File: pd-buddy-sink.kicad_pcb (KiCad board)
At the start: 4 copper layers, 30 x 25 mm, 43 parts, among them J1 5-20 V⎓, J2 USB_C_Receptacle, P1 SWD, Q1 MMBT2222ALT1G, Q2 DMP4015SSS, SW1 Boot, SW2 Setup, U1 AP2204R-3.3TRG1, U2 STM32F072C8Ux, U3 FUSB302BMPX

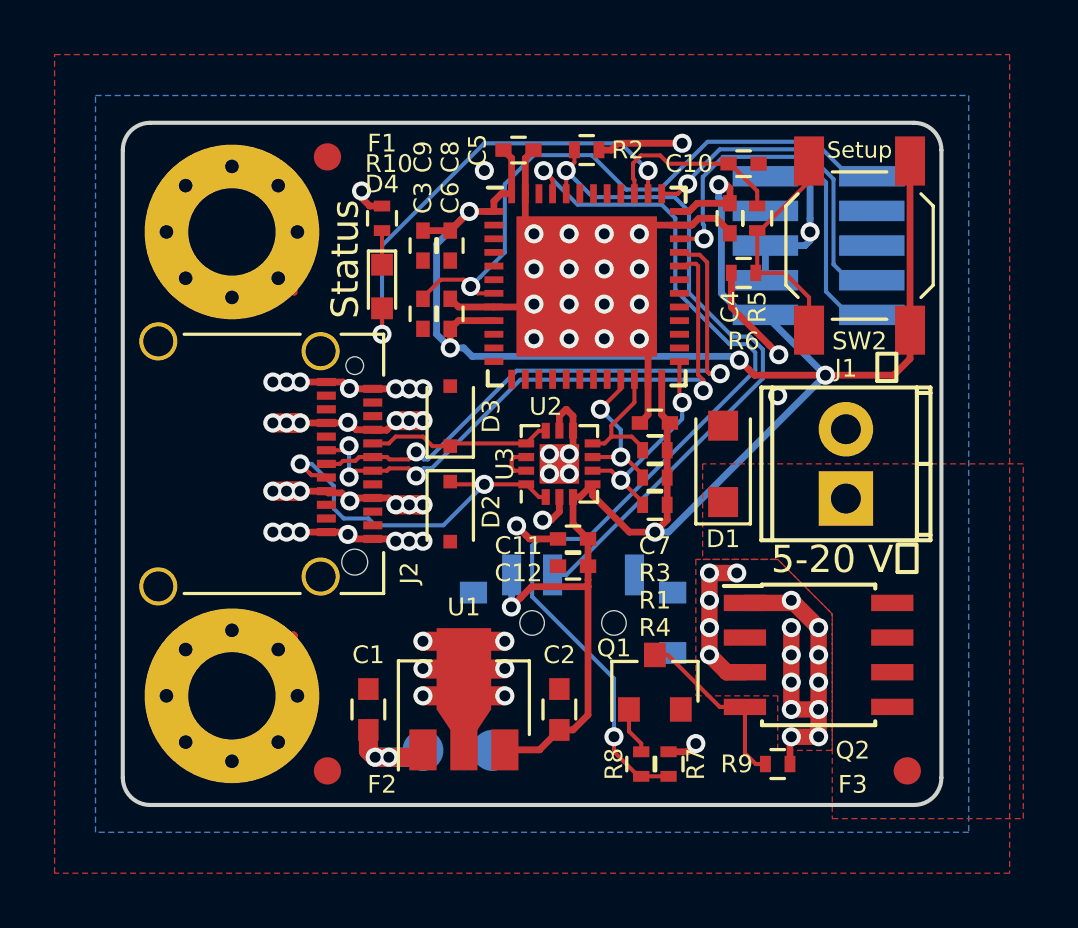
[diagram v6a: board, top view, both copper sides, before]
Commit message: Change part for D2 and D3
Now they're MM3Z5V6T1G, an SOD-323 5.6 V 300 mW Zener diode.  Similar to
the old part, but easier to solder and cheaper.  One of those two points
matters.
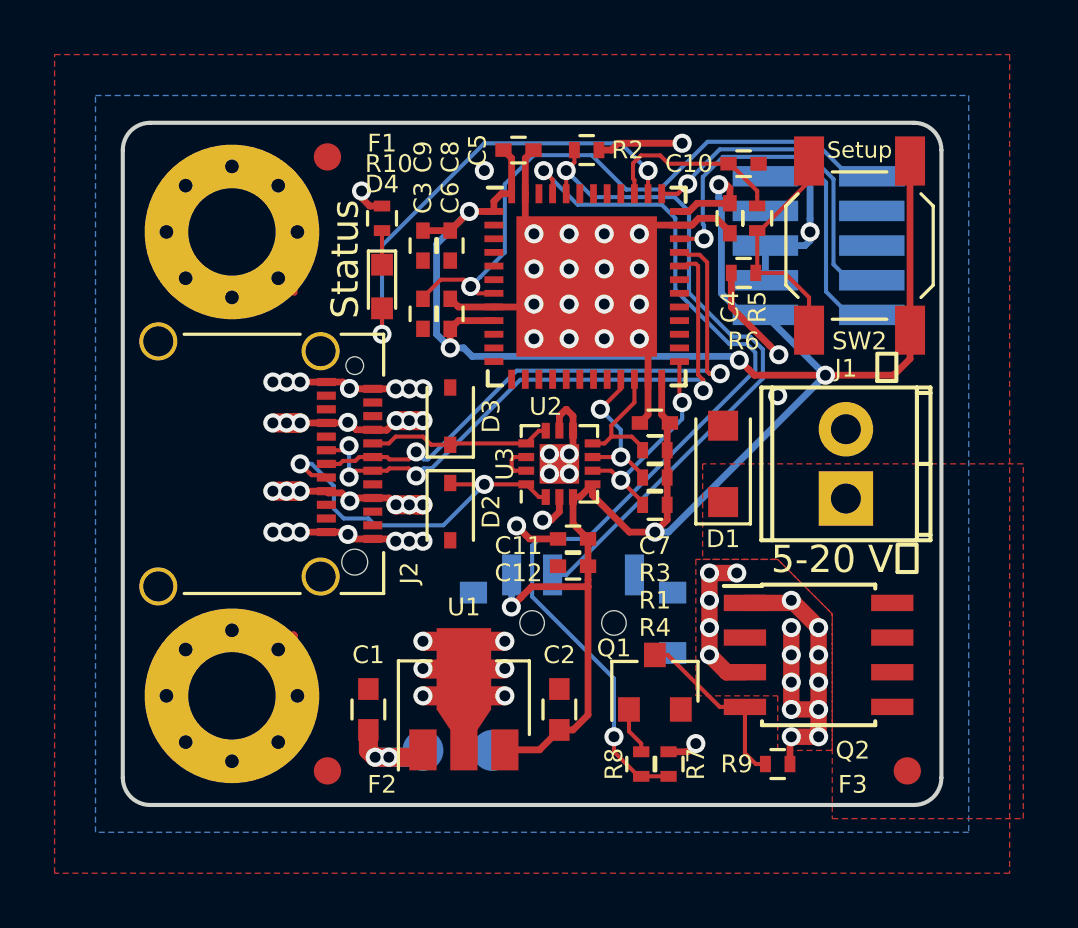
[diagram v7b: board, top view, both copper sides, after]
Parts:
- D2, D3: value CZRF52C5V6 -> MM3Z5V6T1G; footprint Diodes_SMD:D_SOD-323F -> Diodes_SMD:D_SOD-323
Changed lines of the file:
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@@
       (net 2 GND))
   )
-  (module Diodes_SMD:D_SOD-323F (layer F.Cu)
+  (module Diodes_SMD:D_SOD-323 (layer F.Cu)
     (at 93.5 71.75 270)
-    (descr "SOD-323F http://www.nxp.com/documents/outline_drawing/SOD323F.pdf")
-    (tags SOD-323F)
+    (descr SOD-323)
+    (tags SOD-323)
     (attr smd)
-    (fp_text reference D2 (at 0 -1.5 450) (layer F.SilkS)
+    (fp_text reference D2 (at 0 -1.5 270) (layer F.SilkS)
       (effects (font (size 0.65 0.65) (thickness 0.12)))
     )
-    (fp_text value CZRF52C5V6 (at 0.1 1.9 270) (layer F.Fab)
+    (fp_text value MM3Z5V6T1G (at 0.1 1.9 270) (layer F.Fab)
       (effects (font (size 1 1) (thickness 0.15)))
     )
@@
     (fp_line (start -1.5 0.85) (end 1.05 0.85) (layer F.SilkS) (width 0.12))
     (fp_line (start -1.5 -0.85) (end 1.05 -0.85) (layer F.SilkS) (width 0.12))
-    (pad 1 smd rect (at -1.1 0 270) (size 0.5 0.5) (layers F.Cu F.Paste F.Mask)
+    (pad 1 smd rect (at -1.05 0 270) (size 0.6 0.45) (layers F.Cu F.Paste F.Mask)
       (net 5 "/PD PHY/CC2"))
-    (pad 2 smd rect (at 1.1 0 270) (size 0.5 0.5) (layers F.Cu F.Paste F.Mask)
+    (pad 2 smd rect (at 1.05 0 270) (size 0.6 0.45) (layers F.Cu F.Paste F.Mask)
       (net 2 GND))
-    (model ${KISYS3DMOD}/Diodes_SMD.3dshapes/D_SOD-323F.wrl
+    (model ${KISYS3DMOD}/Diodes_SMD.3dshapes/D_SOD-323.wrl
       (at (xyz 0 0 0))
       (scale (xyz 1 1 1))
@@
     )
   )
-  (module Diodes_SMD:D_SOD-323F (layer F.Cu)
+  (module Diodes_SMD:D_SOD-323 (layer F.Cu)
     (at 93.5 68.25 90)
-    (descr "SOD-323F http://www.nxp.com/documents/outline_drawing/SOD323F.pdf")
-    (tags SOD-323F)
+    (descr SOD-323)
+    (tags SOD-323)
     (attr smd)
     (fp_text reference D3 (at 0 1.5 90) (layer F.SilkS)
       (effects (font (size 0.65 0.65) (thickness 0.12)))
     )
-    (fp_text value CZRF52C5V6 (at 0.1 1.9 90) (layer F.Fab)
+    (fp_text value MM3Z5V6T1G (at 0.1 1.9 90) (layer F.Fab)
       (effects (font (size 1 1) (thickness 0.15)))
     )
@@
     (fp_line (start -1.5 0.85) (end 1.05 0.85) (layer F.SilkS) (width 0.12))
     (fp_line (start -1.5 -0.85) (end 1.05 -0.85) (layer F.SilkS) (width 0.12))
-    (pad 1 smd rect (at -1.1 0 90) (size 0.5 0.5) (layers F.Cu F.Paste F.Mask)
+    (pad 1 smd rect (at -1.05 0 90) (size 0.6 0.45) (layers F.Cu F.Paste F.Mask)
       (net 6 "/PD PHY/CC1"))
-    (pad 2 smd rect (at 1.1 0 90) (size 0.5 0.5) (layers F.Cu F.Paste F.Mask)
+    (pad 2 smd rect (at 1.05 0 90) (size 0.6 0.45) (layers F.Cu F.Paste F.Mask)
       (net 2 GND))
-    (model ${KISYS3DMOD}/Diodes_SMD.3dshapes/D_SOD-323F.wrl
+    (model ${KISYS3DMOD}/Diodes_SMD.3dshapes/D_SOD-323.wrl
       (at (xyz 0 0 0))
       (scale (xyz 1 1 1))
@@
   (segment (start 94.5 63.75) (end 95.1 63.75) (width 0.15) (layer F.Cu) (net 4))
   (via (at 94.25 63.5) (size 0.7) (drill 0.4) (layers F.Cu B.Cu) (net 4))
-  (segment (start 94.75 70.75) (end 93.6 70.75) (width 0.15) (layer F.Cu) (net 5))
-  (segment (start 93.6 70.75) (end 93.5 70.65) (width 0.15) (layer F.Cu) (net 5))
+  (segment (start 94.75 70.75) (end 93.55 70.75) (width 0.15) (layer F.Cu) (net 5))
+  (segment (start 93.55 70.75) (end 93.5 70.7) (width 0.15) (layer F.Cu) (net 5))
   (segment (start 94.75 70.75) (end 93.25 72.25) (width 0.15) (layer B.Cu) (net 5))
   (segment (start 93.25 72.25) (end 90.75 72.25) (width 0.15) (layer B.Cu) (net 5))
@@
   (segment (start 96.285 70.75) (end 96.75 71.215) (width 0.15) (layer F.Cu) (net 5))
   (segment (start 96.75 71.215) (end 97 71.215) (width 0.15) (layer F.Cu) (net 5))
-  (segment (start 96.285 69.25) (end 93.6 69.25) (width 0.15) (layer F.Cu) (net 6))
-  (segment (start 93.6 69.25) (end 93.5 69.35) (width 0.15) (layer F.Cu) (net 6))
+  (segment (start 96.285 69.25) (end 93.55 69.25) (width 0.15) (layer F.Cu) (net 6))
+  (segment (start 93.55 69.25) (end 93.5 69.3) (width 0.15) (layer F.Cu) (net 6))
+  (segment (start 92.5 69) (end 92.8 69.3) (width 0.15) (layer F.Cu) (net 6))
+  (segment (start 92.8 69.3) (end 93.5 69.3) (width 0.15) (layer F.Cu) (net 6))
   (segment (start 90.66 69.25) (end 91.25 69.25) (width 0.15) (layer F.Cu) (net 6))
   (segment (start 91.25 69.25) (end 91.5 69) (width 0.15) (layer F.Cu) (net 6))
   (segment (start 91.5 69) (end 92.5 69) (width 0.15) (layer F.Cu) (net 6))
-  (segment (start 92.5 69) (end 92.85 69.35) (width 0.15) (layer F.Cu) (net 6))
-  (segment (start 92.85 69.35) (end 93.5 69.35) (width 0.15) (layer F.Cu) (net 6))
   (segment (start 96.285 69.25) (end 96.75 68.785) (width 0.15) (layer F.Cu) (net 6))
   (segment (start 96.75 68.785) (end 97 68.785) (width 0.15) (layer F.Cu) (net 6))

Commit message: Remove fiducial refs and trace between NC pads
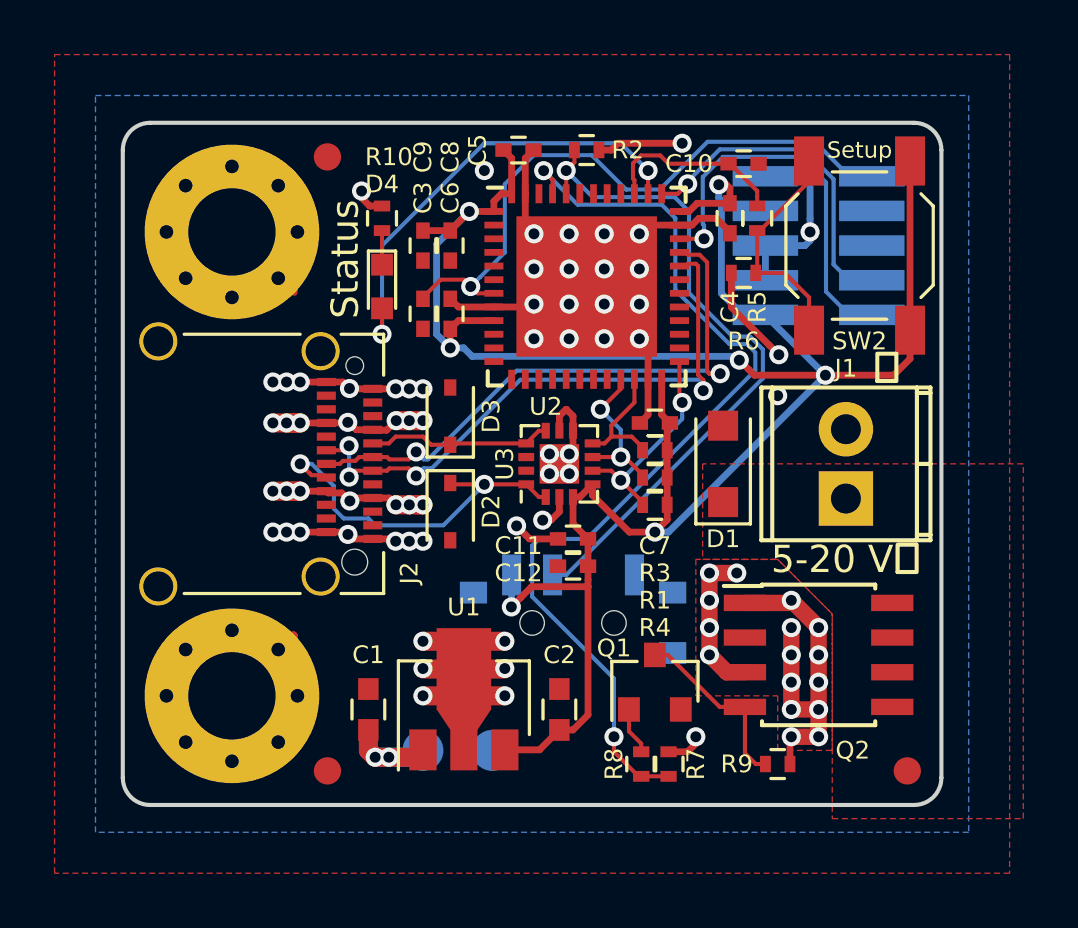
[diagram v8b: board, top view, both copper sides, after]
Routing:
- net Net-(U3-Pad12): track 1.02 -> 0.00 mm
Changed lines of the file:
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@@
     (links 137)
     (no_connects 0)
-    (area 81.424999 57.424999 111.575001 82.575001)
+    (area 72.101904 55 127.148096 85.71)
     (thickness 1.6)
     (drawings 10)
-    (tracks 547)
+    (tracks 543)
     (zones 0)
     (modules 43)
@@
     (pad_drill 0.762)
     (pad_to_mask_clearance 0.0635)
-    (aux_axis_origin 0 0)
+    (aux_axis_origin 81.5 57.5)
+    (grid_origin 81.5 57.5)
     (visible_elements FFFFFF7F)
     (pcbplotparams
@@
     (tags marker)
     (attr virtual)
-    (fp_text reference F3 (at -2 0.5) (layer F.SilkS)
+    (fp_text reference F3 (at -2 0.5) (layer F.SilkS) hide
       (effects (font (size 0.65 0.65) (thickness 0.12)))
     )
@@
     (tags marker)
     (attr virtual)
-    (fp_text reference F2 (at 2 0.5) (layer F.SilkS)
+    (fp_text reference F2 (at 2 0.5) (layer F.SilkS) hide
       (effects (font (size 0.65 0.65) (thickness 0.12)))
     )
@@
     (tags "resistor 0402")
     (attr smd)
-    (fp_text reference R10 (at 2 0.25 180) (layer F.SilkS)
+    (fp_text reference R10 (at 2.25 0.25 180) (layer F.SilkS)
       (effects (font (size 0.65 0.65) (thickness 0.12)))
     )
@@
     (tags marker)
     (attr virtual)
-    (fp_text reference F1 (at 2 -0.5) (layer F.SilkS)
+    (fp_text reference F1 (at 2 -0.5) (layer F.SilkS) hide
       (effects (font (size 0.65 0.65) (thickness 0.12)))
     )
@@
   (segment (start 88.96 71) (end 89.024999 71.064999) (width 0.25) (layer F.Cu) (net 1))
   (segment (start 89.024999 71.064999) (end 89.526102 71.064999) (width 0.25) (layer F.Cu) (net 1))
+  (segment (start 102.2 80.55) (end 102.5 80.25) (width 0.25) (layer F.Cu) (net 2))
+  (segment (start 102.5 80.25) (end 102.5 80) (width 0.25) (layer F.Cu) (net 2))
+  (via (at 102.5 80) (size 0.7) (drill 0.4) (layers F.Cu B.Cu) (net 2))
+  (segment (start 101.5 80.55) (end 102.2 80.55) (width 0.25) (layer F.Cu) (net 2))
   (segment (start 95.14375 59.25) (end 94.75 59.25) (width 0.25) (layer In2.Cu) (net 2))
   (segment (start 96.56875 60.675) (end 95.14375 59.25) (width 0.25) (layer In2.Cu) (net 2))
@@
   (segment (start 106.77 67.5) (end 105.924264 67.5) (width 0.25) (layer In2.Cu) (net 2))
   (via (at 105.5 67.5) (size 0.7) (drill 0.4) (layers F.Cu B.Cu) (net 2))
-  (segment (start 101.5 80.55) (end 102.2 80.55) (width 0.25) (layer F.Cu) (net 2))
-  (segment (start 102.2 80.55) (end 102.5 80.25) (width 0.25) (layer F.Cu) (net 2))
-  (via (at 102.5 80.25) (size 0.7) (drill 0.4) (layers F.Cu B.Cu) (net 2))
   (segment (start 98 68.785) (end 98 69.5) (width 0.25) (layer F.Cu) (net 2))
   (segment (start 98 69.5) (end 97.8625 69.6375) (width 0.25) (layer F.Cu) (net 2))
@@
   (segment (start 91 65.25) (end 91 64.3) (width 0.15) (layer F.Cu) (net 49))
   (via (at 91 65.25) (size 0.7) (drill 0.4) (layers F.Cu B.Cu) (net 49))
-  (segment (start 96.285 69.75) (end 95.845 69.75) (width 0.15) (layer F.Cu) (net 50))
-  (segment (start 95.845 69.75) (end 95.75 69.845) (width 0.15) (layer F.Cu) (net 50))
-  (segment (start 95.75 70.155) (end 95.75 69.845) (width 0.15) (layer F.Cu) (net 50))
-  (segment (start 95.845 70.25) (end 95.75 70.155) (width 0.15) (layer F.Cu) (net 50))
-  (segment (start 96.285 70.25) (end 95.845 70.25) (width 0.15) (layer F.Cu) (net 51))
   (zone (net 2) (net_name GND) (layer B.Cu) (hatch edge 0.508)
     (connect_pads (clearance 0.254))
